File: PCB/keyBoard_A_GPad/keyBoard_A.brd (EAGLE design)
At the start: 488.3 x 222.2 mm, 429 parts, among them IC1 74HC04N, IC2 LMV358IDGKR, J1 J, J10 J, J11 J, J12 J, J13 J, J14 J, J15 J, J16 J, J17 J, J18 J, J19 J, J2 J, J20 J, J21 J, J22 J, J23 J, J24 J, J25 J, J26 J, J27 J, J28 J, J29 J, J3 J, J30 J, J31 J, J32 J, J33 J, J34 J, J35 J, J36 J, J37 J, J38 J, J39 J, J4 J, J40 J, J41 J, J42 J, J43 J, J44 J, J45 J, J47 USB MICRO, J5 J, J6 J, J7 J, J8 J, J9 J, Y1 16MHz KX-7, Y2 16MHz KX-7

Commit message: add kesize table. bad pcb a b
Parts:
- removed U$100, U$101, U$102, U$103, U$104, U$105, U$106, U$107, U$108, U$109, U$110, U$111, U$113, U$166, U$167, U$168, U$169, U$170, U$171, U$172, U$173, U$174, U$175, U$176, U$179, U$184, U$185, U$188: (no value), kbmx:18X18
- removed U$177: (no value), kbmx:18X52
- removed U$178, U$183: (no value), kbmx:18X37
- removed U$180, U$181, U$182: (no value), kbmx:18X23
- removed U$186: (no value), kbmxco:SIZE132
- removed U$187: (no value), kbmx:18X42
- removed U$189, U$190: (no value), kbmx:18X28
- added 2D1: 74HC138N, detali2:DIL16
- added 2D2: 74HC04N, detali2:DIL14
- added C19: 100n, rcl:C0805
- added C20: 100n, rcl:C1206
- added D49, D50, D51, D52, D53, D54, D55, D56, D57, D58, D59, D60, D61, D62, D63, D64, D64B, D65, D66, D67, D67B, D68, D69, D70, D71, D72, D73, D74, D75, D76, D77, D78, D79, D80, D81, D82, D83, D84, D85, D86, D87, D88, D89, D92, D93: LL4148, detali:SOD80C
- added J46, J48, J49, J50, J51, J52, J53, J54, J55, J56, J57, J58, J59, J60, J61, J62, J63, J64, J65, J66, J67, J68, J69, J70, J71, J72, J73, J74, J75, J76, J77, J78, J79, J80, J81, J82, J83, J84, J85, J86, J87, J88, J89, J90, J91, J92, J93, J94, J95, J96: (no value), detali2:R1206W
- added JA47, JA48, JA49, JA50, JA51, JA52, JA53, JA54, JA55, JA56, JA57, JA58, JA59, JA60, JA61, JA62, JA63, JA64, JA65, JA66, JA67, JA67B, JA67B1, JA68, JA69, JA70, JA71, JA72, JA73, JA74, JA74B, JA75, JA76, JA77, JA78, JA79, JA80, JA81, JA82, JA83, JA84, JA85, JA86, JA87, JB47, JB48, JB49, JB50, JB51, JB52, JB53, JB54, JB55, JB56, JB57, JB58, JB59, JB60, JB61, JB62, JB63, JB64, JB65, JB66, JB67, JB67B, JB68, JB69, JB70, JB71, JB72, JB73, JB74, JB74B, JB75, JB76, JB77, JB78, JB79, JB80, JB81, JB82, JB83, JB84, JB85, JB86, JB87: (no value), detali:SJ
- added R16: 1k, rcl:R0805
- added R17, R18, R19, R21, R22: 10k, rcl:R0805
- added R20: 10k, rcl:R1206W
- added S47: F7, cherrymx:CHERRY-MX-4P
- added S48: F8, cherrymx:CHERRY-MX-4P
- added S49: F9, cherrymx:CHERRY-MX-4P
- added S50: F10, cherrymx:CHERRY-MX-4P
- added S51: F11, cherrymx:CHERRY-MX-4P
- added S52: F12, cherrymx:CHERRY-MX-4P
- added S53: 7, cherrymx:CHERRY-MX-4P
- added S54: 8, cherrymx:CHERRY-MX-4P
- added S55: 9, cherrymx:CHERRY-MX-4P
- added S56: 0, cherrymx:CHERRY-MX-4P
- added S57: -, cherrymx:CHERRY-MX-4P
- added S58: =, cherrymx:CHERRY-MX-4P
- added S59: BS, cherrymx:CHERRY-MX-4P
- added S60: Y, cherrymx:CHERRY-MX-4P
- added S61: U, cherrymx:CHERRY-MX-4P
- added S62: I, cherrymx:CHERRY-MX-4P
- added S63: O, cherrymx:CHERRY-MX-4P
- added S64: P, cherrymx:CHERRY-MX-4P
- added S65: [, cherrymx:CHERRY-MX-4P
- added S66: ], cherrymx:CHERRY-MX-4P
- added S67: |d, cherrymx:CHERRY-MX-4P
- added S67B: |u, cherrymx:CHERRY-MX
- added S67C: |, cherrymx:CHERRY-MX-4P
- added S68: H, cherrymx:CHERRY-MX-4P
- added S69: J, cherrymx:CHERRY-MX-4P
- added S70: K, cherrymx:CHERRY-MX-4P
- added S71: L, cherrymx:CHERRY-MX-4P
- added S72: :, cherrymx:CHERRY-MX-4P
- added S73: ", cherrymx:CHERRY-MX-4P
- added S74: Del, cherrymx:CHERRY-MX-4P
- added S74A: Enter, cherrymx:CHERRY-MX-4P
- added S74B: Enter, cherrymx:CHERRY-MX
- added S75: N, cherrymx:CHERRY-MX-4P
- added S76: M, cherrymx:CHERRY-MX-4P
- added S77: <, cherrymx:CHERRY-MX-4P
- added S78: >, cherrymx:CHERRY-MX-4P
- added S79: ~, cherrymx:CHERRY-MX-4P
- added S80: ?, cherrymx:CHERRY-MX-4P
- added S81: R Shift, cherrymx:CHERRY-MX-4P
- added S82: Space, cherrymx:CHERRY-MX-4P
- added S83: FN3, cherrymx:CHERRY-MX-4P
- added S84: R_Alt, cherrymx:CHERRY-MX-4P
- added S85: RCtrl, cherrymx:CHERRY-MX-4P
- added S86: PrtScr, cherrymx:CHERRY-MX-4P
- added S87: FN2, cherrymx:CHERRY-MX-4P
- added SV4: CON_KB_B, detali2:FE12
- added U$116, U$117, U$53, U$54, U$55, U$56, U$57, U$58, U$59, U$60, U$61, U$62, U$63, U$64, U$65, U$66, U$67, U$68, U$69, U$70, U$71, U$72, U$73, U$74, U$75, U$76, U$77, U$78, U$79, U$80, U$83, U$84, U$85, U$86, U$89: (no value), kbmx:18X18
- added U$165: (no value), kbmxco:SIZE132
- added U$87: (no value), kbmx:18X52
- added U$90, U$92: (no value), kbmx:18X23
- U$88: device kbmx:18X18 -> kbmx:18X37
- U$93, U$98: device kbmx:18X18 -> kbmx:18X23
- U$94: device kbmx:18X18 -> kbmx:18X42
- U$96: device kbmx:18X18 -> kbmx:18X28
- U$97: device kbmx:18X18 -> kbmxco:SIZE132
- moved U$98 141.9 mm to (338.0, -331.3)
- moved U$97 132.4 mm to (267.8, -370.6), turned to 90 degrees
- moved U$88 120.4 mm to (325.9, -274.1)
- moved U$99 108.0 mm to (334.2, -291.9)
- moved U$93 107.8 mm to (254.2, -350.3)
- moved U$95 105.1 mm to (273.9, -349.0)
- moved U$96 82.0 mm to (340.5, -293.2)
- moved U$94 75.5 mm to (328.5, -312.2)
- moved U$91 4.62 mm to (73.7, -354.3)
- moved U$17 3.18 mm to (158.8, -349.9)
- moved U$16 2.54 mm to (120.7, -349.9)
- moved U$15 1.91 mm to (97.2, -349.9)
- moved S44 0.64 mm to (98.4, -349.9)
- moved S46 0.63 mm to (161.9, -349.2)
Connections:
- new net +3VD: 2D2.14, C20.1, D92.C
- new net 2I: 2D1.14, D50.C, J95.1
- new net 8J: D79.C, D84.C, D85.C, D89.C, J87.1
- new net G1: 2D2.9, JA47.2, JA48.2, JA49.2, JA53.2, JA60.2, JA68.2, JA75.2, JA82.2, R17.2
- new net G2: J63.2, JA54.2, JA55.2, JA56.2, JA61.2, JA69.2, JA70.2, JA76.2, JA77.2, R18.2
- new net G3: J57.2, JA62.2, JA63.2, JA71.2
- new net G4: J76.2, JA50.2, JA51.2, JA57.2, JA64.2, JA72.2, JA78.2, JA79.2, JA87.2
- new net G5: J62.2, JA52.2, JA58.2, JA65.2, JA66.2, JA73.2, JA80.2, JA83.2, JA84.2
- new net G6: J59.2, JA59.2, JA67.2, JA67B.2, JA67B1.2, JA74B.2, JA81.2, JA85.2, JA86.2, JB74.1
- new net GG5: 2D2.11, J61.1, R21.2
- new net N$107: JB52.2, S52.SW1
- new net N$151: JB63.2, S63.SW1
- new net N$229: JB74.2, S74A.SW1, S74B.SW1
- new net N$230: JA74.1, S74A.SW2, S74B.SW2
- new net N$233: JB47.2, S47.SW1
- new net N$234: JB53.2, S53.SW1
- new net N$235: JB60.2, S60.SW1
- new net N$236: JB68.2, S68.SW1
- new net N$237: JB75.2, S75.SW1
- new net N$238: JB82.2, S82.SW1
- new net N$239: JB48.2, S48.SW1
- new net N$240: JB54.2, S54.SW1
- new net N$241: JB61.2, S61.SW1
- new net N$242: JB69.2, S69.SW1
- new net N$243: JB49.2, S49.SW1
- new net N$244: JB55.2, S55.SW1
- new net N$245: JB70.2, S70.SW1
- new net N$246: JB77.2, S77.SW1
- new net N$247: JB56.2, S56.SW1
- new net N$248: JB51.2, S51.SW1
- new net N$249: D49.A, JB47.1
- new net N$250: D55.A, JB53.1
- new net N$251: D62.A, JB60.1
- new net N$252: D70.A, JB68.1
- new net N$253: D77.A, JB75.1
- new net N$254: D84.A, JB82.1
- new net N$255: D50.A, JB48.1
- new net N$256: D56.A, JB54.1
- new net N$257: D63.A, JB61.1
- new net N$258: D71.A, JB69.1
- new net N$259: D78.A, JB76.1
- new net N$260: D85.A, JB83.1
- new net N$261: D51.A, JB49.1
- new net N$262: D57.A, JB55.1
- new net N$263: D64.A, JB62.1
- new net N$264: D72.A, JB70.1
- new net N$265: D79.A, JB77.1
- new net N$266: D86.A, JB84.1
- new net N$267: D52.A, JB50.1
- new net N$268: D58.A, JB56.1
- new net N$269: D65.A, JB63.1
- new net N$270: D73.A, JB71.1
- new net N$271: D80.A, JB78.1
- new net N$272: D87.A, JB85.1
- new net N$274: D53.A, JB51.1
- new net N$275: D59.A, JB57.1
- new net N$277: D66.A, JB64.1
- new net N$278: D74.A, JB72.1
- new net N$279: D81.A, JB79.1
- new net N$280: D88.A, JB86.1
- new net N$281: D54.A, JB52.1
- new net N$282: D60.A, JB58.1
- new net N$283: D67.A, JB65.1
- new net N$285: D75.A, JB73.1
- new net N$286: D82.A, JB80.1
- new net N$287: D61.A, JB59.1
- new net N$288: D68.A, JB66.1
- new net N$289: D69.A, JB67.1
- new net N$290: D83.A, JB81.1
- new net N$291: JA47.1, S47.SW2
- new net N$292: JA53.1, S53.SW2
- new net N$293: JA60.1, S60.SW2
- new net N$294: JA68.1, S68.SW2
- new net N$295: JA75.1, S75.SW2
- new net N$296: JA82.1, S82.SW2
- new net N$297: JA48.1, S48.SW2
- new net N$298: JA54.1, S54.SW2
- new net N$299: JA61.1, S61.SW2
- new net N$300: JA69.1, S69.SW2
- new net N$301: JA49.1, S49.SW2
- new net N$302: JA55.1, S55.SW2
- new net N$303: JA70.1, S70.SW2
- new net N$304: JA77.1, S77.SW2
- new net N$305: JA56.1, S56.SW2
- new net N$306: JA63.1, S63.SW2
- new net N$307: JA51.1, S51.SW2
- new net N$308: JA52.1, S52.SW2
- new net N$309: D64B.A, JB74B.1
- new net N$310: JA67B1.1, S67B.SW2
- new net N$311: JA67B.1, S67C.SW1
- new net N$312: D76.A, JA74.2
- new net N$313: JB67.2, S67.SW2
- new net N$314: JA67.1, S67.SW1
- new net N$315: JB81.2, S81.SW2
- new net N$316: JA81.1, S81.SW1
- new net N$317: JB59.2, S59.SW2
- new net N$318: JA59.1, S59.SW1
- new net N$319: JB85.2, S85.SW2
- new net N$320: JA85.1, S85.SW1
- new net N$321: JB74B.2, S74.SW2
- new net N$322: JA74B.1, S74.SW1
- new net N$323: J96.1, S67B.SW1, S67C.SW2
- new net N$324: JA87.1, S87.SW1
- new net N$325: JB87.2, S87.SW2
- new net N$326: D89.A, JB87.1
- new net N$327: JB50.2, S50.SW2
- new net N$328: JA50.1, S50.SW1
- new net N$329: JB78.2, S78.SW2
- new net N$330: JA78.1, S78.SW1
- new net N$331: D67B.A, JB67B.1
- new net N$332: JB58.2, S58.SW2
- new net N$333: JB65.2, S65.SW2
- new net N$334: JA65.1, S65.SW1
- new net N$335: JA58.1, S58.SW1
- new net N$336: JB66.2, S66.SW1
- new net N$337: JA66.1, S66.SW2
- new net N$338: JB79.2, S79.SW2
- new net N$339: JA79.1, S79.SW1
- new net N$340: JB83.2, S83.SW2
- new net N$341: JA83.1, S83.SW1
- new net N$342: JB73.2, S73.SW2
- new net N$343: JA73.1, S73.SW1
- new net N$344: JA80.1, S80.SW1
- new net N$345: JB80.2, S80.SW2
- new net N$346: JB84.2, S84.SW2
- new net N$347: JA84.1, S84.SW1
- new net N$349: JB57.2, S57.SW2
- new net N$350: JA57.1, S57.SW1
- new net N$351: JA64.1, S64.SW1
- new net N$352: JB64.2, S64.SW2
- new net N$353: JB72.2, S72.SW2
- new net N$354: JA72.1, S72.SW1
- new net N$355: J48.1, J49.2
- new net N$356: JB62.2, S62.SW2
- new net N$357: JA62.1, S62.SW1
- new net N$358: JB71.2, S71.SW1
- new net N$359: JA71.1, S71.SW2
- new net N$360: 2D1.6, R16.2
- new net N$361: JB76.2, S76.SW2
- new net N$362: JA76.1, S76.SW1
- new net N$363: 2D2.6, SV4.7
- new net N$364: 2D2.4, SV4.6
- new net N$365: 2D2.2, SV4.5
- new net N$366: 2D2.12, J64.2
- new net N$367: 2D2.8, J69.2
- new net N$368: J57.1, J58.2
- new net N$369: J59.1, J60.2
- new net N$370: 2D2.1, J63.1
- new net N$371: J64.1, SV4.4
- new net N$372: J65.1, SV4.3
- new net N$373: J65.2, J66.1
- new net N$374: 2D2.10, J66.2
- new net N$375: J67.1, SV4.2
- new net N$376: J67.2, J68.1
- new net N$377: J68.2, J69.1
- new net N$378: D92.A, D93.C
- new net N$379: J70.1, J73.2
- new net N$380: J71.1, J74.2
- new net N$381: J72.1, J75.2
- new net N$382: J73.1, J77.2
- new net N$383: J74.1, J78.2
- new net N$384: J75.1, J79.2
- new net N$385: J79.1, J80.2
- new net N$386: J77.1, J81.2
- new net N$387: J78.1, J82.2
- new net N$388: J80.1, J83.2
- new net N$389: J82.1, J84.2
- new net N$391: J81.1, J85.2
- new net N$392: 2D1.1, J83.1
- new net N$393: 2D1.2, J84.1
- new net N$394: 2D1.3, J85.1
- new net N$395: 2D1.15, J86.2
- new net N$396: JB86.2, S86.SW1
- new net N$397: JA86.1, S86.SW2
- new net N$398: 2D1.7, J88.2
- new net N$399: J90.1, J91.2
- new net N$400: 2D1.11, J90.2
- new net N$401: J89.2, J92.1
- new net N$402: J93.1, J94.2
- new net N$403: 2D1.9, J93.2
- new net N$404: 2D1.10, J92.2
- new net N$405: J46.1, J95.2
- new net N$406: J96.2, JB67B.2
- new net PG3: 2D2.3, J58.1, R19.2
- new net PG4: 2D2.5, J76.1, R20.2
- new net PG5: J61.2, J62.1
- new net PG6: 2D2.13, J60.1, R22.2
- net +5V: now also 2D1.16, C19.1, D93.A, R16.1, R17.1, R18.1, R19.1, R20.1, R21.1, R22.1, SV4.11
- net 1: now also D51.C, D52.C, D54.C, D58.C, D64B.C, J86.1
- net 2: now also D53.C, D60.C, D61.C, J46.2, J53.2
- net 2J: now also D57.C, J53.1
- net 3: now also D49.C, D56.C, D59.C, D65.C, J48.2
- net 3J: now also D67B.C, D68.C, J49.1, J88.1
- net 4: now also D67.C, D76.C, J50.1, J91.1
- net 4J: now also D66.C, D73.C, J50.2, J54.2
- net 4J2: now also D55.C, D63.C, J54.1
- net 5: now also D69.C, D75.C, J51.1, J89.1
- net 5J: now also D62.C, D64.C, D71.C, D74.C, J51.2
- net 6: now also D81.C, D82.C, D83.C, J55.2, J94.1
- net 6J2: now also D72.C, J55.1, J56.2
- net 6J3: now also D70.C, J56.1
- net 7: now also 2D1.13, D86.C, D87.C, J52.1
- net 7J: now also D77.C, D78.C, D80.C, J52.2
- net 8: now also 2D1.12, D88.C, J87.2
- net D1: now also J70.2, SV4.10
- net D2: now also J71.2, SV4.9
- net D3: now also J72.2, SV4.8
- net GND: now also 2D1.4, 2D1.5, 2D1.8, 2D2.7, C19.2, C20.2, SV4.1
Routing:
- net G6: track 0.00 -> 216.4 mm
- net 7: track 25.2 -> 239.8 mm
- net GND: track 301.7 -> 500.8 mm
- net +5V: track 152.8 -> 349.6 mm, vias 13 -> 16
- net G1: track 0.00 -> 196.4 mm
- net 2I: track 0.00 -> 169.8 mm
- net G5: track 0.00 -> 169.5 mm
- net G4: track 0.00 -> 169.4 mm
- net G2: track 0.00 -> 146.4 mm
- net 1: track 31.8 -> 169.3 mm
- net 8J: track 0.00 -> 136.6 mm
- net 8: track 115.4 -> 241.1 mm
- net N$369: track 0.00 -> 97.8 mm, vias 1 -> 0
- net 5J: track 24.7 -> 118.3 mm
- net N$403: track 0.00 -> 92.6 mm
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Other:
- outline, holes or cut-outs redrawn

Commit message: new pcb >
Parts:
- removed 1D0: ATMEGA32U4, detali_main:SMARTPRJ_TQFP44-PAD
- removed C1, C2: 22p, SmartPrj:C0603-ROUND
- removed R1: 1M, SmartPrj:R0603-ROUND
- removed R2, R7: (no value), rcl:M0805
- removed S74B: Enter, cherrymx:CHERRY-MX
- removed SV1: (no value), detali_main:FE12
- removed SV2: CON_KB_N, detali_main:FE09
- removed U$117, U$119, U$120, U$121, U$122, U$123, U$124, U$125, U$126, U$127, U$128, U$129, U$130, U$131, U$132, U$133, U$134, U$135, U$136, U$137, U$138, U$139, U$141: (no value), kbmx:18X18
- removed U$140: (no value), kbmx:37X18
- removed U$142, U$143, U$144, U$145, U$146, U$147, U$148, U$150, U$151, U$152, U$153, U$154, U$155, U$156, U$157, U$158, U$159, U$160, U$161, U$162, U$163, U$164: (no value), kbmxco:KEY
- removed U$149: (no value), kbmxco:NUMENTER
- removed Y2: 16MHz KX-7, SmartPrj:CRYSTAL-3.2-2.5
- added 1D2: ATMEGA32U4, detali_main:SMARTPRJ_TQFP44-PAD
- added C21, C23: 22p, SmartPrj:C0603-ROUND
- added R23, R25: (no value), rcl:M0805
- added R24: 1M, SmartPrj:R0603-ROUND
- added S44A: Fn1, cherrymx:CHERRY-MX
- added SV5: CON_KB_N, detali_main:FE09
- added SV6: (no value), detali_main:FE12
- added U$101: (no value), kbmx:18X18
- added U$102: FE1.1S, imcom:FE1.1S_SSOP-28
- added U$103: (no value), kbmx:18X23
- added U$105: (no value), kbmx:18X42
- added Y3: 16MHz KX-7, SmartPrj:CRYSTAL-3.2-2.5
- S44: value F1 -> FN1
- U$52: value FE1.1S -> (none); device imcom:FE1.1S_SSOP-28 -> kbmx:18X42
- U$81: value (none) -> CHERRY-MX; device kbmx:18X18 -> cherrymx:CHERRY-MX
- U$98: device kbmx:18X23 -> kbmx:18X18
- moved U$82 387.8 mm to (57.1, -348.6)
- moved U$52 285.5 mm to (325.1, -330.8)
- moved U$98 243.2 mm to (95.6, -351.2), turned to 90 degrees
- moved U$81 221.2 mm to (214.9, -349.9), turned to 180 degrees
- moved U$88 85.3 mm to (401.0, -233.7)
- moved S67 57.7 mm to (313.1, -273.7)
- moved JA67 57.1 mm to (321.0, -276.2)
- moved JB67 52.9 mm to (312.7, -281.6), turned to 270 degrees
- moved U$15 41.8 mm to (127.0, -379.1)
- moved D69 39.5 mm to (306.4, -288.6), turned to 270 degrees
- moved C13 38.5 mm to (143.2, -450.5)
- moved C14 38.5 mm to (145.1, -466.4)
- moved L1 38.5 mm to (175.6, -454.3)
- moved C11 38.5 mm to (145.1, -461.3)
- moved C12 38.5 mm to (145.7, -473.4)
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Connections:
- removed net N$117: JA44.1, S44.SW2
- removed net N$197: 1D0.33, R2.1
- removed net N$284: 1D0.12, R7.1
- removed net N$65: JB44.2, S44.SW1
- removed net XTAL3: 1D0.16, C1.2, R1.2, Y2.3
- removed net XTAL4: 1D0.17, C2.1, R1.1, Y2.1
- new net +5V_B: 2D1.16, C19.1, D93.A, R16.1, R17.1, R18.1, R19.1, R20.1, R21.1, R22.1, SV4.11
- new net AFN1A: JB44.2, S44.SW1, S44A.SW1
- new net AFN1B: JA44.1, S44.SW2, S44A.SW2
- new net B1: D51.C, D52.C, D54.C, D58.C, D64B.C, J86.1
- new net B2: D53.C, D60.C, D61.C, J46.2, J53.2
- new net B2J: D57.C, J53.1
- new net B3: D49.C, D56.C, D59.C, D65.C, J48.2
- new net B3J: D67B.C, D68.C, J49.1, J88.1
- new net B4: D67.C, D76.C, J50.1, J91.1
- new net B4J: D66.C, D73.C, J50.2, J54.2
- new net B4J2: D55.C, D63.C, J54.1
- new net B5: D69.C, D75.C, J51.1, J89.1
- new net B5J: D62.C, D64.C, D71.C, D74.C, J51.2
- new net B6: D81.C, D82.C, D83.C, J55.2, J94.1
- new net B6J2: D72.C, J55.1, J56.2
- new net B6J3: D70.C, J56.1
- new net B7: 2D1.13, D86.C, D87.C, J52.1
- new net B7J: D77.C, D78.C, D80.C, J52.2
- new net B8: 2D1.12, D88.C, J87.2
- new net BD1: J70.2, SV4.10
- new net BD2: J71.2, SV4.9
- new net BD3: J72.2, SV4.8
- new net CD1: SV5.8, SV6.10
- new net CD2: SV5.7, SV6.9
- new net CD3: SV5.6, SV6.8
- new net GND_B: 2D1.4, 2D1.5, 2D1.8, 2D2.7, C19.2, C20.2, SV4.1
- new net N$506: 1D2.12, R23.1
- new net N$507: 1D2.33, R25.1
- new net XTAL5: 1D2.16, C21.2, R24.2, Y3.3
- new net XTAL6: 1D2.17, C23.1, R24.1, Y3.1
- net +5V: now also R25.2, SV5.9, SV6.11; no longer 2D1.16, C19.1, D93.A, R16.1, R17.1, R18.1, R19.1, R2.2, R20.1, R21.1, R22.1, SV1.11, SV2.9, SV4.11
- net 1: no longer D51.C, D52.C, D54.C, D58.C, D64B.C, J86.1
- net 2: no longer D53.C, D60.C, D61.C, J46.2, J53.2
- net 2J: no longer D57.C, J53.1
- net 3: no longer D49.C, D56.C, D59.C, D65.C, J48.2
- net 3J: no longer D67B.C, D68.C, J49.1, J88.1
- net 4: no longer D67.C, D76.C, J50.1, J91.1
- net 4J: no longer D66.C, D73.C, J50.2, J54.2
- net 4J2: no longer D55.C, D63.C, J54.1
- net 5: no longer D69.C, D75.C, J51.1, J89.1
- net 5J: no longer D62.C, D64.C, D71.C, D74.C, J51.2
- net 6: no longer D81.C, D82.C, D83.C, J55.2, J94.1
- net 6J2: no longer D72.C, J55.1, J56.2
- net 6J3: no longer D70.C, J56.1
- net 7: no longer 2D1.13, D86.C, D87.C, J52.1
- net 7J: no longer D77.C, D78.C, D80.C, J52.2
- net 8: no longer 2D1.12, D88.C, J87.2
- net AREF: now also 1D2.42; no longer 1D0.42
- net AVCC: now also 1D2.24; no longer 1D0.24
- net AVCC1: now also 1D2.44; no longer 1D0.44
- net D1: no longer J70.2, SV1.10, SV2.8, SV4.10
- net D2: no longer J71.2, SV1.9, SV2.7, SV4.9
- net D3: no longer J72.2, SV1.8, SV2.6, SV4.8
- net GND: now also 1D2.15, C21.1, C23.2, SV5.1, SV6.1, Y3.2, Y3.4; no longer 1D0.15, 2D1.4, 2D1.5, 2D1.8, 2D2.7, C1.1, C19.2, C2.2, C20.2, SV1.1, SV2.1, SV4.1, Y2.2, Y2.4
- net GND1: now also 1D2.23; no longer 1D0.23
- net GND2: now also 1D2.35; no longer 1D0.35
- net GND3: now also 1D2.43; no longer 1D0.43
- net KBB1: now also SV6.2; no longer SV1.2
- net KBB2: now also SV6.3; no longer SV1.3
- net KBB3: now also SV6.4; no longer SV1.4
- net KBB4: now also SV6.5; no longer SV1.5
- net KBB5: now also SV6.6; no longer SV1.6
- net KBB6: now also SV6.7; no longer SV1.7
- net KBN1: now also SV5.2; no longer SV2.2
- net KBN2: now also SV5.3; no longer SV2.3
- net KBN3: now also SV5.5; no longer SV2.5
- net LED_NUM: now also SV5.4; no longer SV2.4
- net N$229: no longer S74B.SW1
- net N$230: no longer S74B.SW2
- net N$238: now also U$81.SW2
- net N$296: now also U$81.SW1
- net PAD: now also 1D2.P$1; no longer 1D0.P$1
- net UGND: now also 1D2.5; no longer 1D0.5
- net UVCC: now also 1D2.2; no longer 1D0.2
- net VCC: now also 1D2.14; no longer 1D0.14
- net VCC1: now also 1D2.34; no longer 1D0.34
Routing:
- net 7: track 239.8 -> 25.2 mm
- net B7: track 0.00 -> 212.2 mm
- net GND: track 500.8 -> 301.7 mm
- net +5V: track 349.6 -> 152.8 mm, vias 16 -> 13
- net +5V_B: track 0.00 -> 192.7 mm, vias 0 -> 3
- net GND_B: track 0.00 -> 192.2 mm
- net B1: track 0.00 -> 137.4 mm
- net 1: track 169.3 -> 31.8 mm
- net 8: track 241.1 -> 115.4 mm
- net B8: track 0.00 -> 119.4 mm
- net B5J: track 0.00 -> 93.6 mm
- net 5J: track 118.3 -> 24.7 mm
- net B3: track 0.00 -> 84.3 mm
- net 3: track 139.4 -> 55.1 mm
- net 7J: track 116.8 -> 43.7 mm
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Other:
- board size 488.3 x 222.2 mm -> 366 x 253 mm
- board text removed: "1176-16"

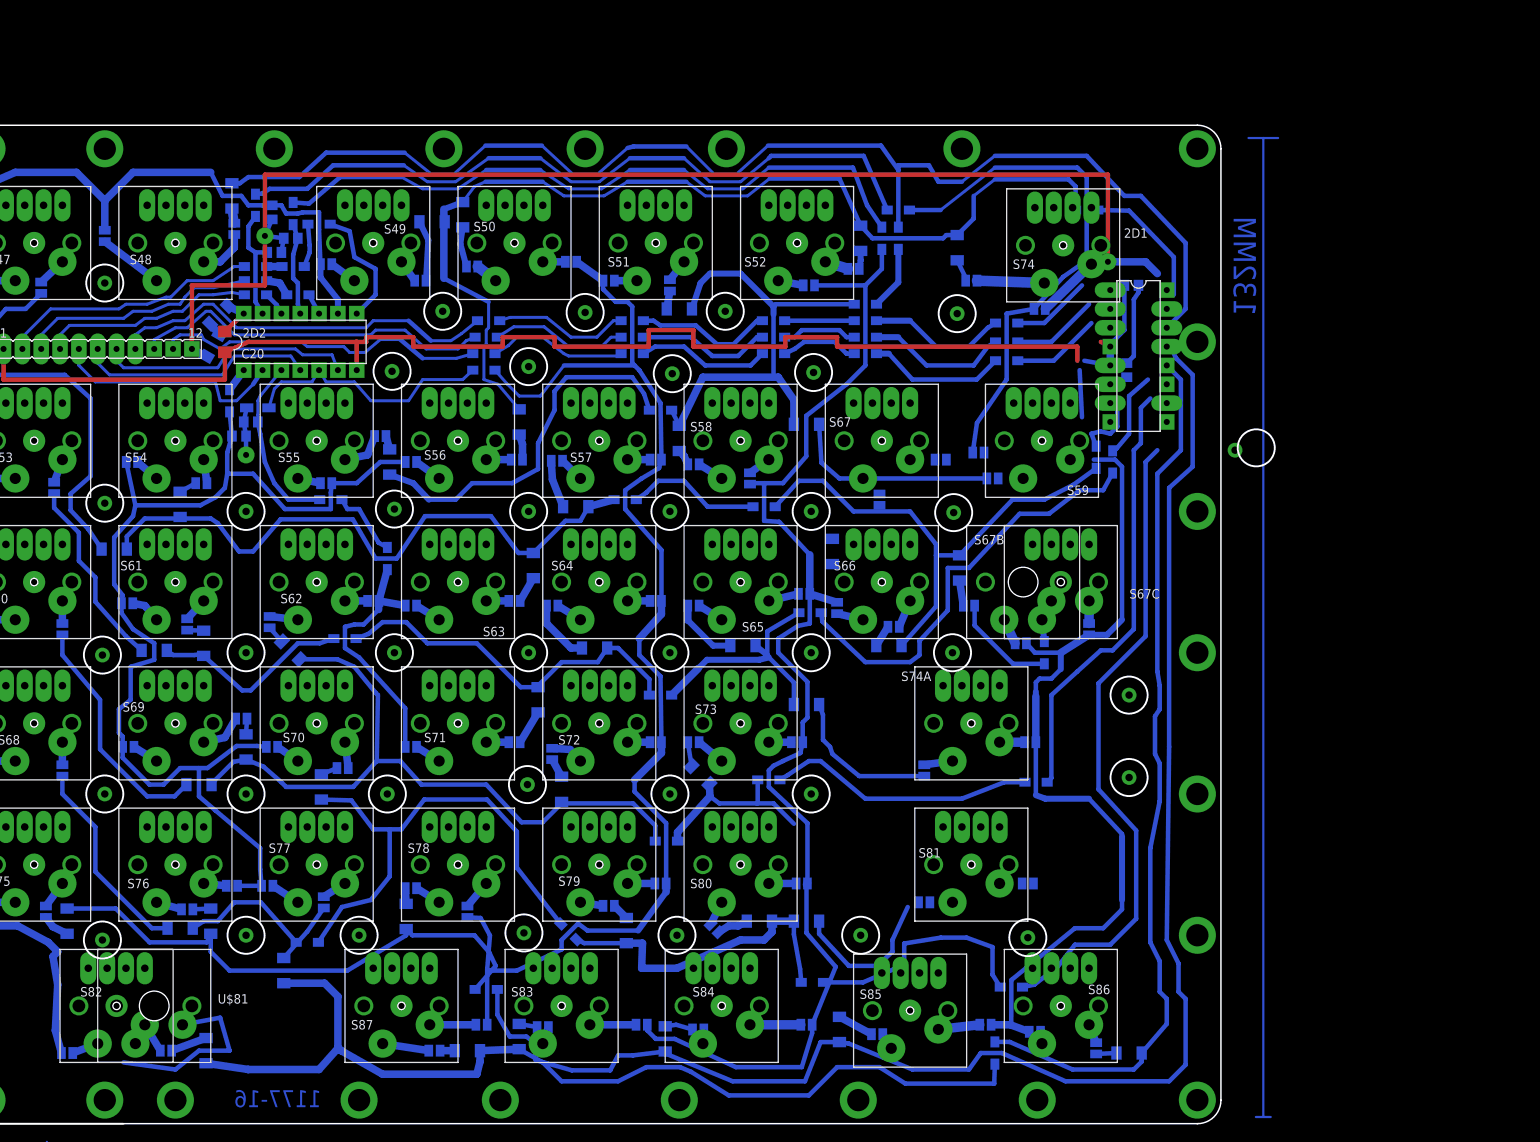
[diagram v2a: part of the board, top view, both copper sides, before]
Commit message: pcb b > ab
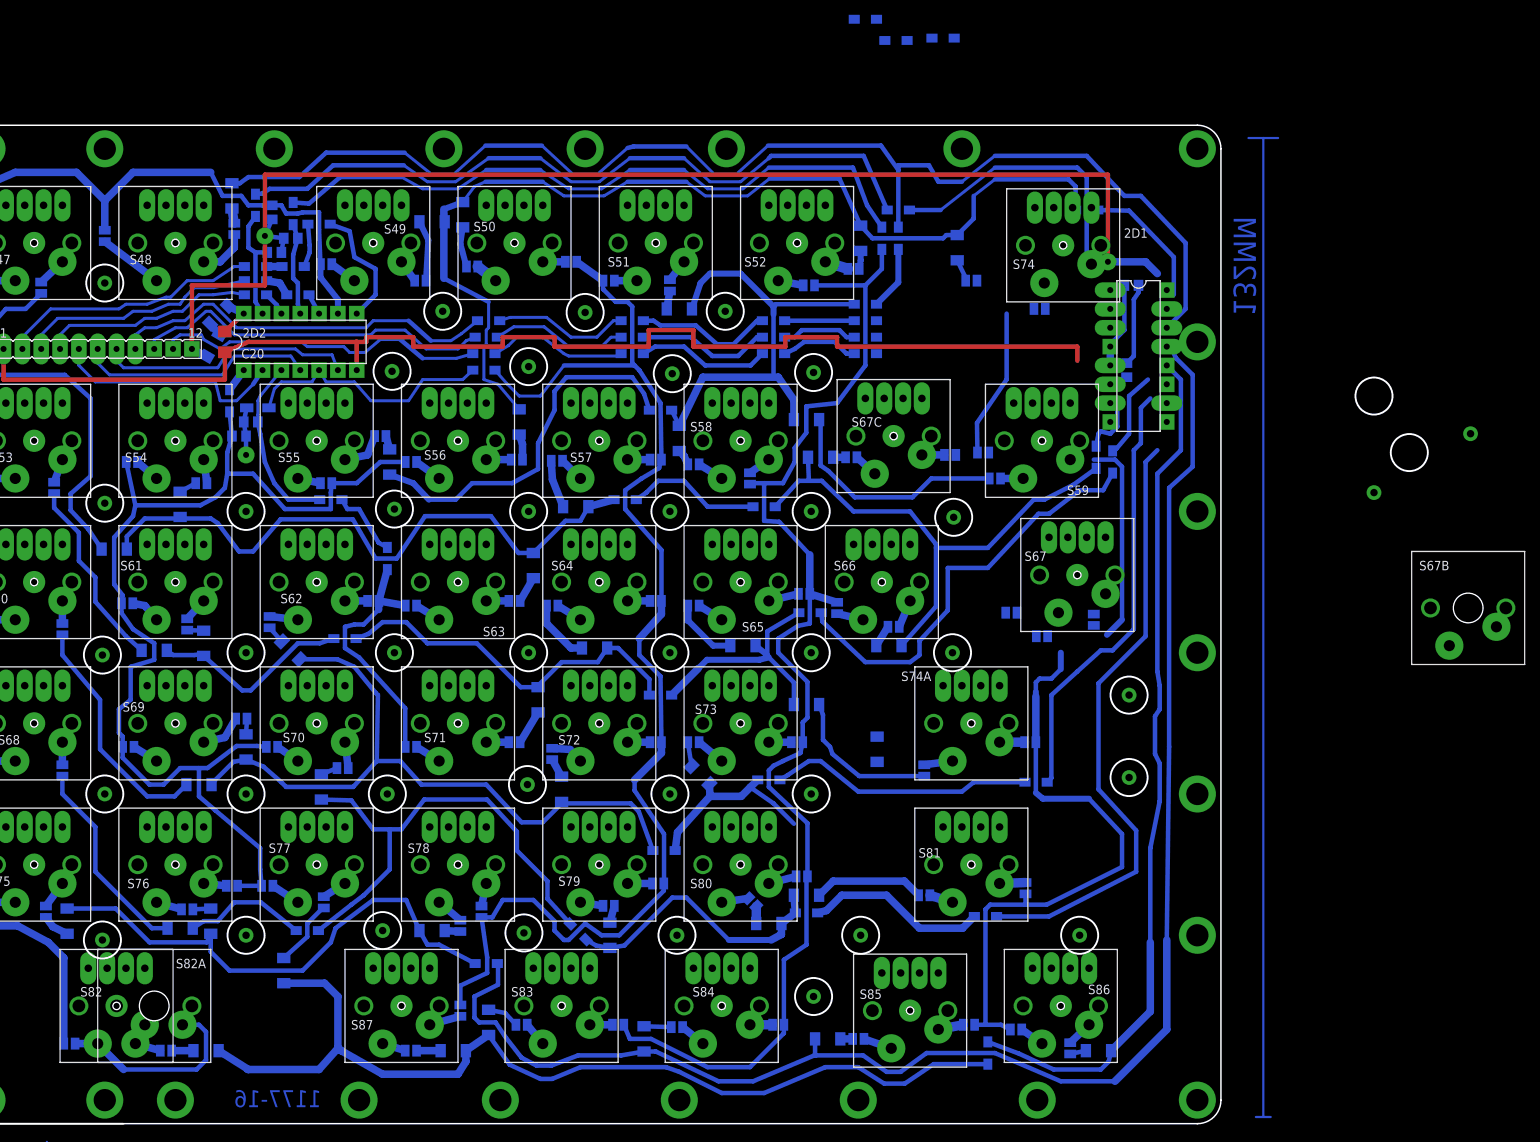
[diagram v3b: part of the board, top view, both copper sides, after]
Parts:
- removed J96: (no value), detali2:R1206W
- S67C: value | -> |u
- S82A: value CHERRY-MX -> space
- moved S67B 60.1 mm to (392.1, -296.2)
- moved J83 45.2 mm to (310.8, -216.9)
- moved J85 44.3 mm to (321.3, -219.4)
- moved J84 43.3 mm to (315.0, -219.7)
- moved S67 32.0 mm to (339.4, -291.8)
- moved JA67B 30.0 mm to (322.3, -275.6), turned to 180 degrees
- moved S67C 29.9 mm to (314.6, -273.1)
- moved JA67 29.9 mm to (341.6, -297.8), turned to 90 degrees
- moved D69 27.3 mm to (312.4, -315.3)
- moved JB67B 25.5 mm to (308.9, -275.9)
- moved D67B 23.9 mm to (304.8, -275.9), turned to 180 degrees
- moved JB67 23.4 mm to (330.5, -296.9), turned to 180 degrees
- moved J93 10.1 mm to (327.0, -337.8)
- moved J94 9.40 mm to (302.9, -337.3)
- moved JB78 8.38 mm to (256.2, -339.1), turned to 270 degrees
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- renumbered U$81 to S82A
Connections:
- removed net N$310: JA67B1.1, S67B.SW2
- removed net N$323: J96.1, S67B.SW1, S67C.SW2
- net N$406: now also S67C.SW2; no longer J96.2
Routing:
- net G6: track 186.3 -> 166.8 mm
- net N$389: track 19.1 -> 0.00 mm
- net N$388: track 18.7 -> 0.00 mm
- net N$391: track 18.6 -> 0.00 mm
- net N$394: track 12.0 -> 0.00 mm
- net N$393: track 11.7 -> 0.00 mm
- net GND_B: track 192.2 -> 180.8 mm
- net N$406: track 14.2 -> 3.28 mm
- net N$392: track 10.8 -> 0.00 mm
- net N$321: track 9.09 -> 0.00 mm
- net N$322: track 8.67 -> 0.00 mm
- net N$402: track 32.1 -> 24.5 mm
- net B6: track 44.0 -> 38.1 mm
- net N$323: track 5.80 -> 0.00 mm
- net N$290: track 20.7 -> 15.0 mm
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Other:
- board size 366 x 253 mm -> 386.7 x 253 mm
